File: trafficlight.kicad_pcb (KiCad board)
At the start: 2 copper layers, 17 x 50 mm, 7 parts

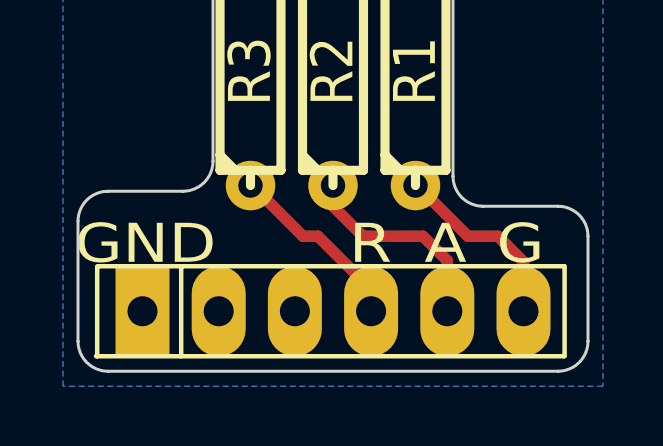
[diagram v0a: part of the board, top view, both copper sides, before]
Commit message: Changed LEDs so that we have separate red, amber and green types. This makes the 3D view look right. Needed extra .wrl file for the red one, and will need another if we add blue LEDs.
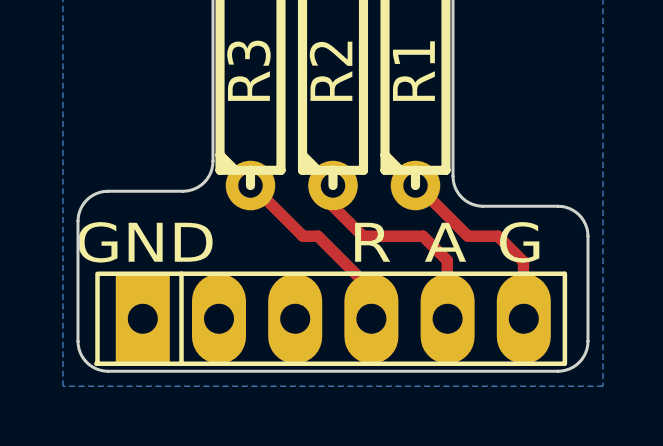
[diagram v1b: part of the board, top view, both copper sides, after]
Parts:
- D1: footprint LED-10MM -> LED-G-10MM
- D2: footprint LED-10MM -> LED-A-10MM
- D3: footprint LED-10MM -> LED-R-10MM
- R1, R2, R3: value (none) -> 330R
- moved ? 0.25 mm to (207.0, 158.8)
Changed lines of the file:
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@@
       (effects (font (size 1.397 1.27) (thickness 0.2032)))
     )
-    (fp_text value "" (at 0 0 90) (layer F.SilkS) hide
+    (fp_text value 330R (at 0 0 90) (layer F.SilkS) hide
       (effects (font (size 1.397 1.27) (thickness 0.2032)))
     )
@@
       (effects (font (size 1.397 1.27) (thickness 0.2032)))
     )
-    (fp_text value "" (at 0 0 90) (layer F.SilkS) hide
+    (fp_text value 330R (at 0 0 90) (layer F.SilkS) hide
       (effects (font (size 1.397 1.27) (thickness 0.2032)))
     )
@@
       (effects (font (size 1.397 1.27) (thickness 0.2032)))
     )
-    (fp_text value "" (at 0 0 90) (layer F.SilkS) hide
+    (fp_text value 330R (at 0 0 90) (layer F.SilkS) hide
       (effects (font (size 1.397 1.27) (thickness 0.2032)))
     )
@@
     )
   )
-  (module LED-10MM (layer F.Cu)
+  (module HDR-6-HORIZ-L (layer F.Cu)
+    (at 207.01 158.75)
+    (descr "Pin header connector 6 pins horiz")
+    (tags "CONN DEV HORIZ 2.54mm")
+    (fp_text reference "" (at 0 -3) (layer F.SilkS)
+      (effects (font (size 1.72974 1.08712) (thickness 0.27178)))
+    )
+    (fp_text value "" (at 0 -5.5) (layer F.SilkS)
+      (effects (font (size 1.524 1.016) (thickness 0.254)))
+    )
+    (fp_line (start -7.9 1.5) (end 7.7 1.5) (layer F.SilkS) (width 0.15))
+    (fp_line (start -7.8 -1.5) (end 7.7 -1.5) (layer F.SilkS) (width 0.15))
+    (fp_text user "" (at 6.35 -2.54) (layer F.SilkS)
+      (effects (font (size 2 2) (thickness 0.15)))
+    )
+    (fp_text user "" (at -6.27 -2.7) (layer F.SilkS)
+      (effects (font (size 2 2) (thickness 0.15)))
+    )
+    (fp_line (start -5.06 1.5) (end -5.06 -1.5) (layer F.SilkS) (width 0.15))
+    (fp_line (start 7.72 1.5) (end 7.72 -1.5) (layer F.SilkS) (width 0.15))
+    (fp_line (start -7.86 -1.5) (end -7.86 1.5) (layer F.SilkS) (width 0.15))
+    (pad 1 thru_hole rect (at -6.35 0) (size 1.8 3) (drill 1)
+      (layers *.Cu *.Mask F.SilkS)
+      (net 4 GND)
+    )
+    (pad 2 thru_hole oval (at -3.81 0) (size 1.8 3) (drill 1)
+      (layers *.Cu *.Mask F.SilkS)
+    )
+    (pad 3 thru_hole oval (at -1.27 0) (size 1.8 3) (drill 1)
+      (layers *.Cu *.Mask F.SilkS)
+    )
+    (pad 4 thru_hole oval (at 1.27 0) (size 1.8 3) (drill 1)
+      (layers *.Cu *.Mask F.SilkS)
+      (net 3 /RED)
+    )
+    (pad 5 thru_hole oval (at 3.81 0) (size 1.8 3) (drill 1)
+      (layers *.Cu *.Mask F.SilkS)
+      (net 1 /AMBER)
+    )
+    (pad 6 thru_hole oval (at 6.35 0) (size 1.8 3) (drill 1)
+      (layers *.Cu *.Mask F.SilkS)
+      (net 2 /GREEN)
+    )
+  )
+  (module LED-G-10MM (layer F.Cu)
     (at 207 139)
-    (descr "LED 10mm - Lead pitch 100mil (2,54mm)")
-    (tags "LED led 10mm 10MM 100mil 2,54mm 2.54mm")
+    (descr "LED 10mm - Lead pitch 100mil (2.54mm)")
+    (tags "LED led amber 10mm 100mil 2.54mm")
     (fp_text reference D1 (at 0 -3) (layer F.SilkS)
       (effects (font (size 0.762 0.762) (thickness 0.0889)))
@@
       (net 4 GND)
     )
-    (model discret/leds/led5_vertical_red.wrl
+    (model discret/leds/led5_vertical_verde.wrl
       (at (xyz 0 0 0))
       (scale (xyz 2 2 2))
@@
     )
   )
-  (module LED-10MM (layer F.Cu)
+  (module LED-A-10MM (layer F.Cu)
     (at 207 128)
-    (descr "LED 10mm - Lead pitch 100mil (2,54mm)")
-    (tags "LED led 10mm 10MM 100mil 2,54mm 2.54mm")
+    (descr "LED 10mm - Lead pitch 100mil (2.54mm)")
+    (tags "LED led amber 10mm 100mil 2.54mm")
     (fp_text reference D2 (at 0 -3) (layer F.SilkS)
       (effects (font (size 0.762 0.762) (thickness 0.0889)))
@@
       (net 4 GND)
     )
-    (model discret/leds/led5_vertical_red.wrl
+    (model discret/leds/led5_vertical_amarelo.wrl
       (at (xyz 0 0 0))
       (scale (xyz 2 2 2))
@@
     )
   )
-  (module LED-10MM (layer F.Cu)
+  (module LED-R-10MM (layer F.Cu)
     (at 207 117)
     (descr "LED 10mm - Lead pitch 100mil (2,54mm)")
@@
       (net 4 GND)
     )
-    (model discret/leds/led5_vertical_red.wrl
+    (model led5_vertical_red.wrl
       (at (xyz 0 0 0))
       (scale (xyz 2 2 2))
@@
     )
   )
-  (module HDR-6-HORIZ-L (layer F.Cu)
-    (at 207 158.5)
-    (descr "Pin header connector 6 pins horiz")
-    (tags "CONN DEV HORIZ 2.54mm")
-    (fp_text reference "" (at 0 -3) (layer F.SilkS)
-      (effects (font (size 1.72974 1.08712) (thickness 0.27178)))
-    )
-    (fp_text value "" (at 0 -5.5) (layer F.SilkS)
-      (effects (font (size 1.524 1.016) (thickness 0.254)))
-    )
-    (fp_line (start -7.9 1.5) (end 7.7 1.5) (layer F.SilkS) (width 0.15))
-    (fp_line (start -7.8 -1.5) (end 7.7 -1.5) (layer F.SilkS) (width 0.15))
-    (fp_line (start -5.06 1.5) (end -5.06 -1.5) (layer F.SilkS) (width 0.15))
-    (fp_line (start 7.72 1.5) (end 7.72 -1.5) (layer F.SilkS) (width 0.15))
-    (fp_line (start -7.86 -1.5) (end -7.86 1.5) (layer F.SilkS) (width 0.15))
-    (pad 1 thru_hole rect (at -6.35 0) (size 1.8 3) (drill 1)
-      (layers *.Cu *.Mask F.SilkS)
-      (net 4 GND)
-    )
-    (pad 2 thru_hole oval (at -3.81 0) (size 1.8 3) (drill 1)
-      (layers *.Cu *.Mask F.SilkS)
-    )
-    (pad 3 thru_hole oval (at -1.27 0) (size 1.8 3) (drill 1)
-      (layers *.Cu *.Mask F.SilkS)
-    )
-    (pad 4 thru_hole oval (at 1.27 0) (size 1.8 3) (drill 1)
-      (layers *.Cu *.Mask F.SilkS)
-      (net 3 /RED)
-    )
-    (pad 5 thru_hole oval (at 3.81 0) (size 1.8 3) (drill 1)
-      (layers *.Cu *.Mask F.SilkS)
-      (net 1 /AMBER)
-    )
-    (pad 6 thru_hole oval (at 6.35 0) (size 1.8 3) (drill 1)
-      (layers *.Cu *.Mask F.SilkS)
-      (net 2 /GREEN)
-    )
-  )

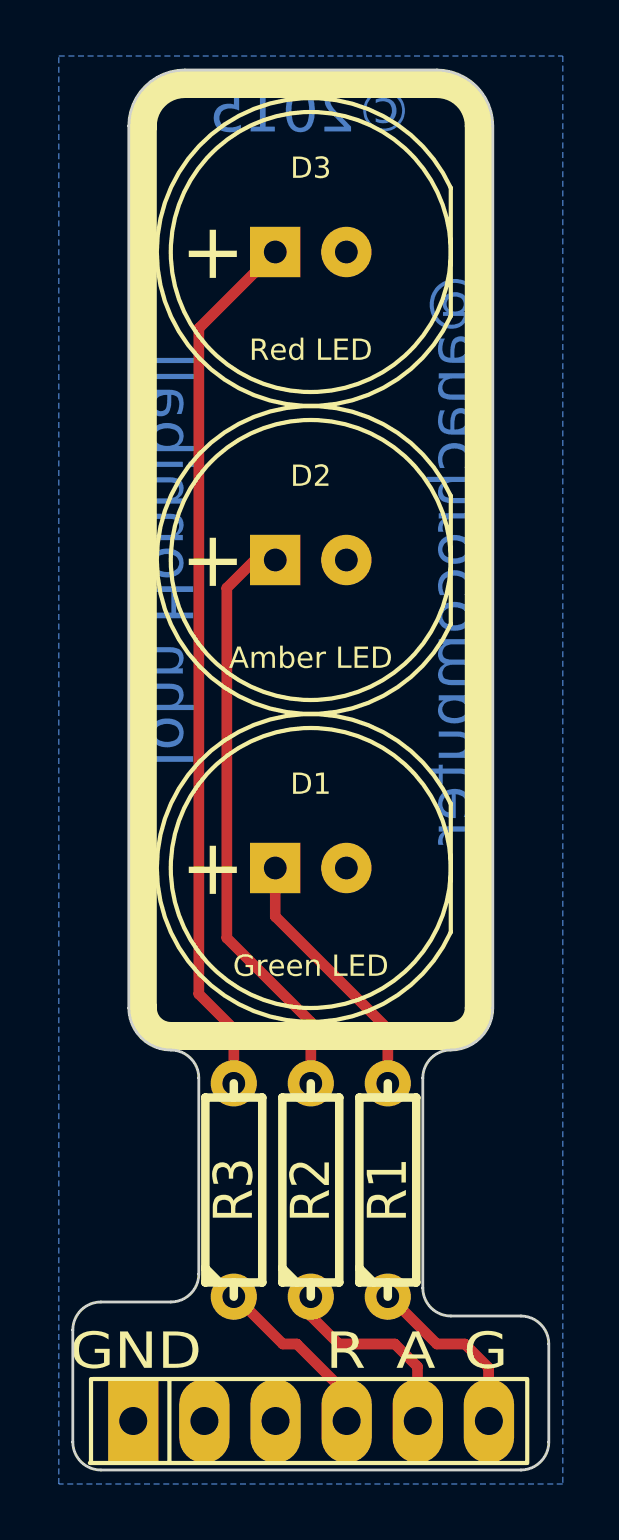
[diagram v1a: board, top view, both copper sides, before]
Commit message: Created new resistor footprints for 0.2in and 0.35in pad spacing. Used them to place one resistor on rear of PCB and bring the other two closer together. This allows the column of the traffic light to be a bit narrower.
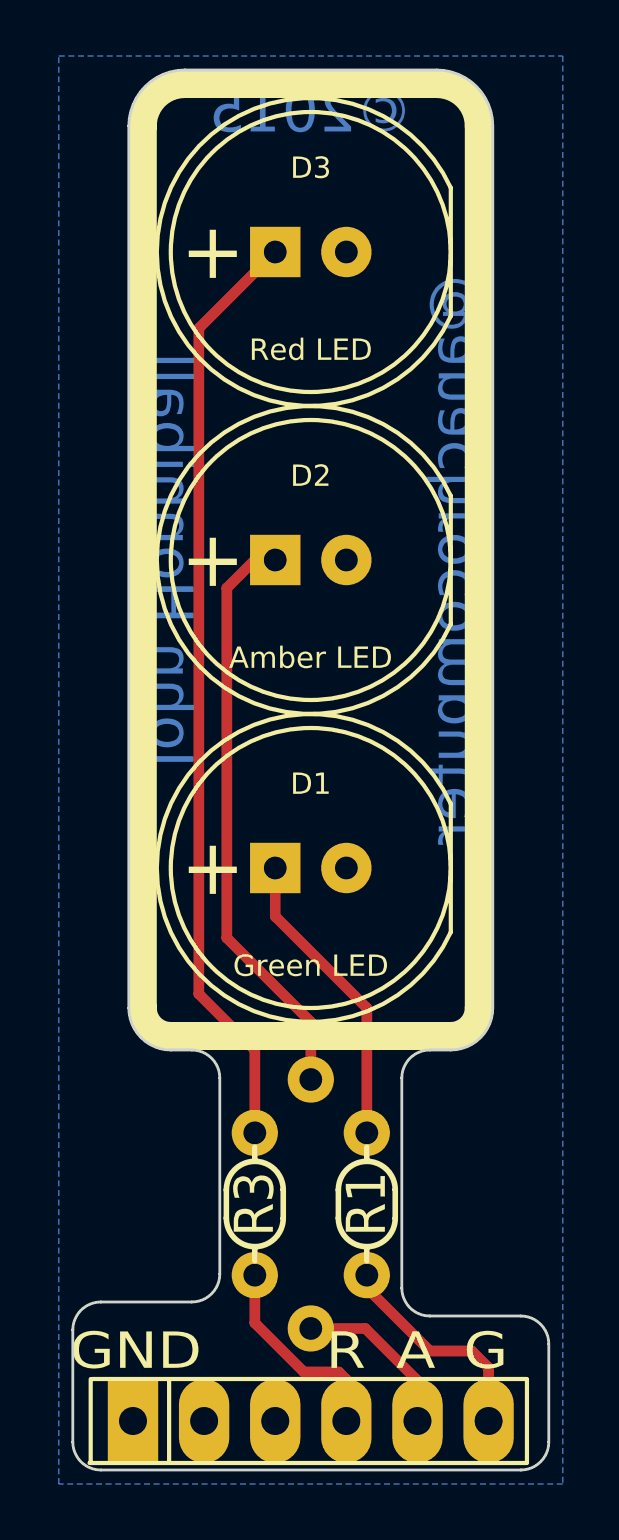
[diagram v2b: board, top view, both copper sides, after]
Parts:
- R1, R3: footprint R3-LARGE_PADS -> R2-LARGE_PADS
- R2: footprint R3-LARGE_PADS -> R3-5-LARGE_PADS; moved to B.Cu
- moved R1 0.90 mm to (209.0, 151.0)
- moved R3 0.90 mm to (205.0, 151.0)
- moved R2 0.50 mm to (207.0, 151.0)
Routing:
- net N-000001: track 31.3 -> 33.4 mm
- net /GREEN: track 6.30 -> 7.89 mm
- net N-000003: track 9.36 -> 10.8 mm
- net /RED: track 6.18 -> 7.30 mm
- net /AMBER: track 6.94 -> 6.02 mm
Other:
- outline, holes or cut-outs redrawn

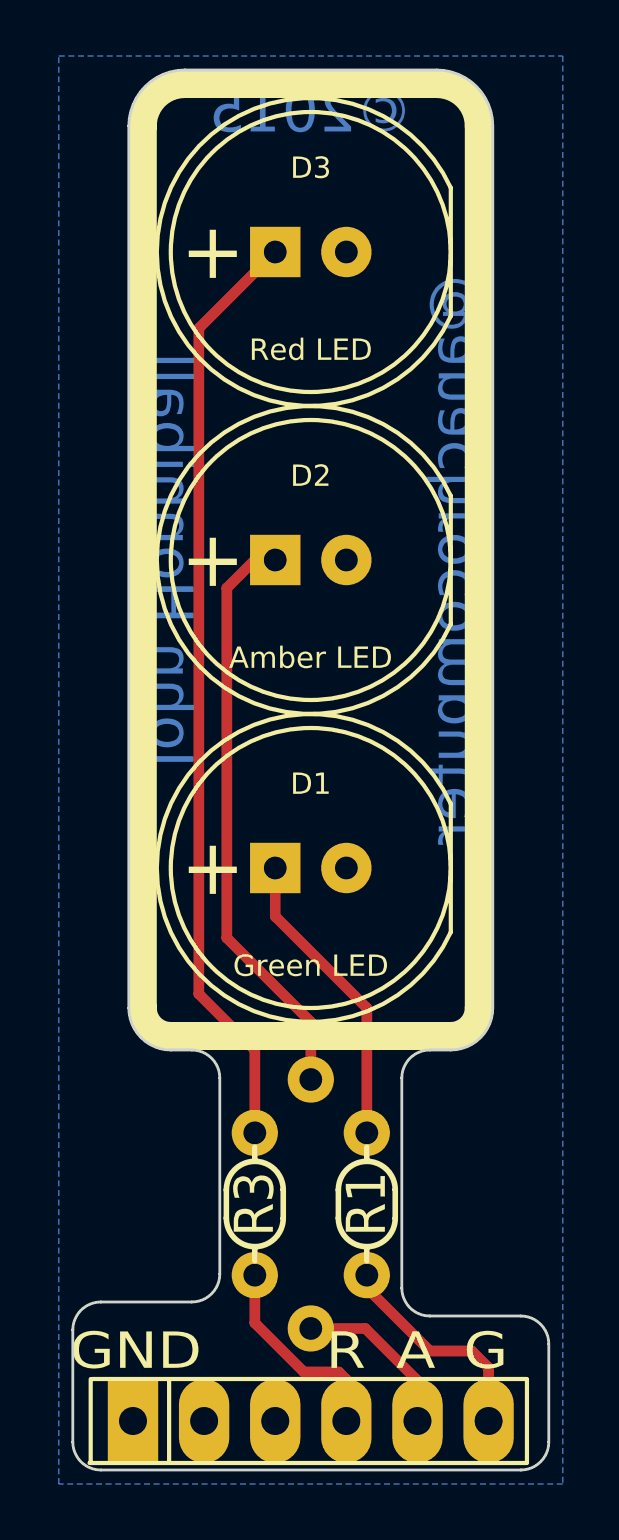
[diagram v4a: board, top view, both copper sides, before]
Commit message: Update to KiCad V6.0.2.
This update renames some of the files. Keep the old ones for now, delete them in a later commit.
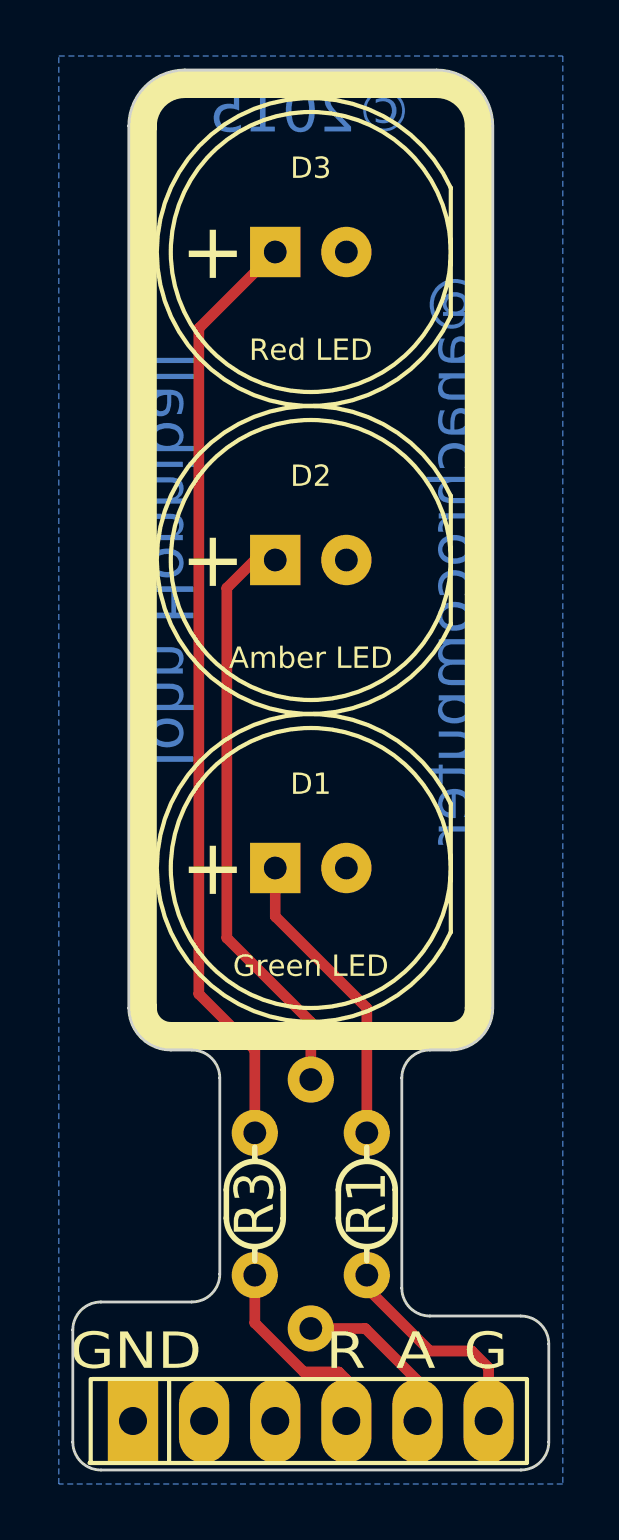
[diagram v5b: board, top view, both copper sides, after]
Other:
- net class Default removed
- net class track removed
